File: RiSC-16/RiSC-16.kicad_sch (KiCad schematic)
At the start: 10 parts, among them U1 74LS283, U2 74LS00, U3 74LS175, U4 74LS257, U5 74LS175

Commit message: Added sheet for register file.
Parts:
- removed C1, C2, C3, C4, C5: 0.1 uF, symbol Device:C_Small_US
- removed U1: 74LS283, symbol 74xx:74LS283
- removed U2: 74LS00, symbol 74xx:74LS00
- removed U3, U5: 74LS175, symbol 74xx:74LS175
- removed U4: 74LS257, symbol 74xx:74LS257
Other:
- added sheet Register File (registers.kicad_sch)
- note removed: "ALU 4-bit slice Four required for ALU"

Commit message: Reworked ALU to use 74LS181 and control signals from Pro. Jacob's reference paper.
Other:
- added sheet Control Unit (control.kicad_sch)
- added sheet Sequencer (sequencer.kicad_sch)
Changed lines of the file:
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@@
+	)
+	(sheet
+		(at 3.81 688.34)
+		(size 290.83 205.74)
+		(exclude_from_sim no)
+		(in_bom yes)
+		(on_board yes)
+		(dnp no)
+		(fields_autoplaced yes)
+		(stroke
+			(width 0.1524)
+			(type solid)
+		)
+		(fill
+			(color 0 0 0 0.0000)
+		)
+		(property "Sheetname" "Sequencer"
+			(at 3.81 687.6284 0)
+			(effects
+				(font
+					(size 1.27 1.27)
+				)
+				(justify left bottom)
+			)
+		)
+		(property "Sheetfile" "sequencer.kicad_sch"
+			(at 3.81 894.6646 0)
+			(effects
+				(font
+					(size 1.27 1.27)
+				)
+				(justify left top)
+			)
+		)
+		(instances
+			(project "RiSC-16"
+				(path "/09ce4153-429f-4803-b069-3af485a81dd6"
+					(page "4")
+				)
+			)
+		)
+	)
+	(sheet
+		(at 5.08 918.21)
+		(size 295.91 195.58)
+		(exclude_from_sim no)
+		(in_bom yes)
+		(on_board yes)
+		(dnp no)
+		(fields_autoplaced yes)
+		(stroke
+			(width 0.1524)
+			(type solid)
+		)
+		(fill
+			(color 0 0 0 0.0000)
+		)
+		(property "Sheetname" "Control Unit"
+			(at 5.08 917.4984 0)
+			(effects
+				(font
+					(size 1.27 1.27)
+				)
+				(justify left bottom)
+			)
+		)
+		(property "Sheetfile" "control.kicad_sch"
+			(at 5.08 1114.3746 0)
+			(effects
+				(font
+					(size 1.27 1.27)
+				)
+				(justify left top)
+			)
+		)
+		(instances
+			(project "RiSC-16"
+				(path "/09ce4153-429f-4803-b069-3af485a81dd6"
+					(page "5")
+				)
+			)
+		)
 	)
 	(sheet

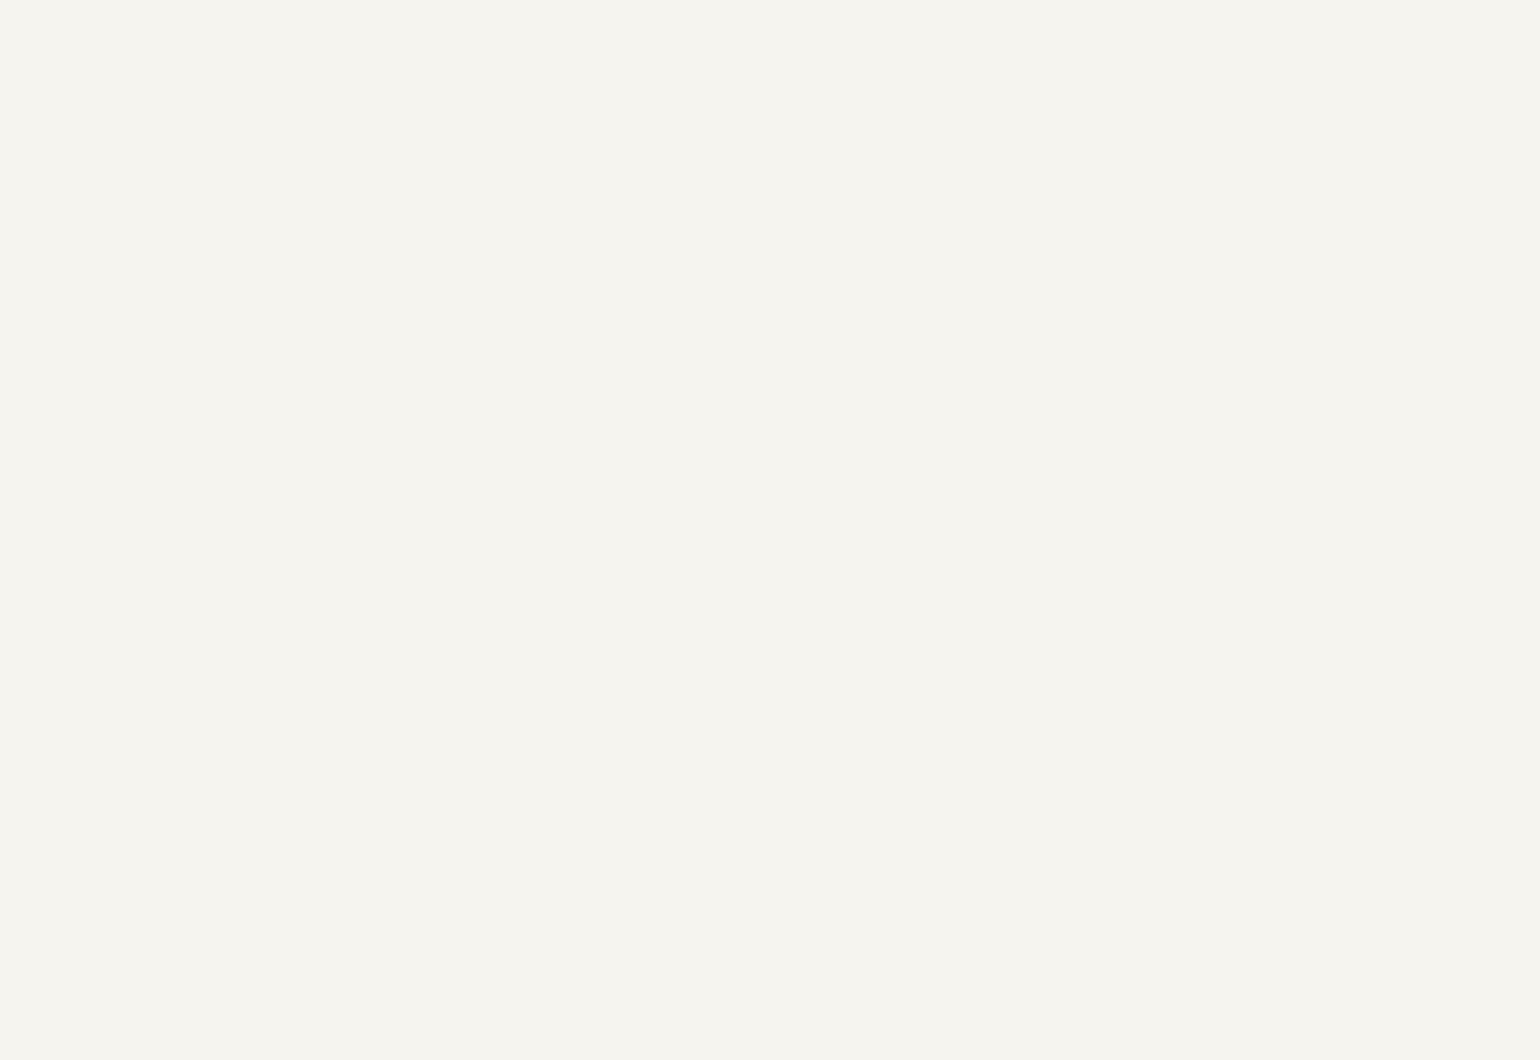
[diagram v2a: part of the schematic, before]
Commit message: Move program ccounter to its own page
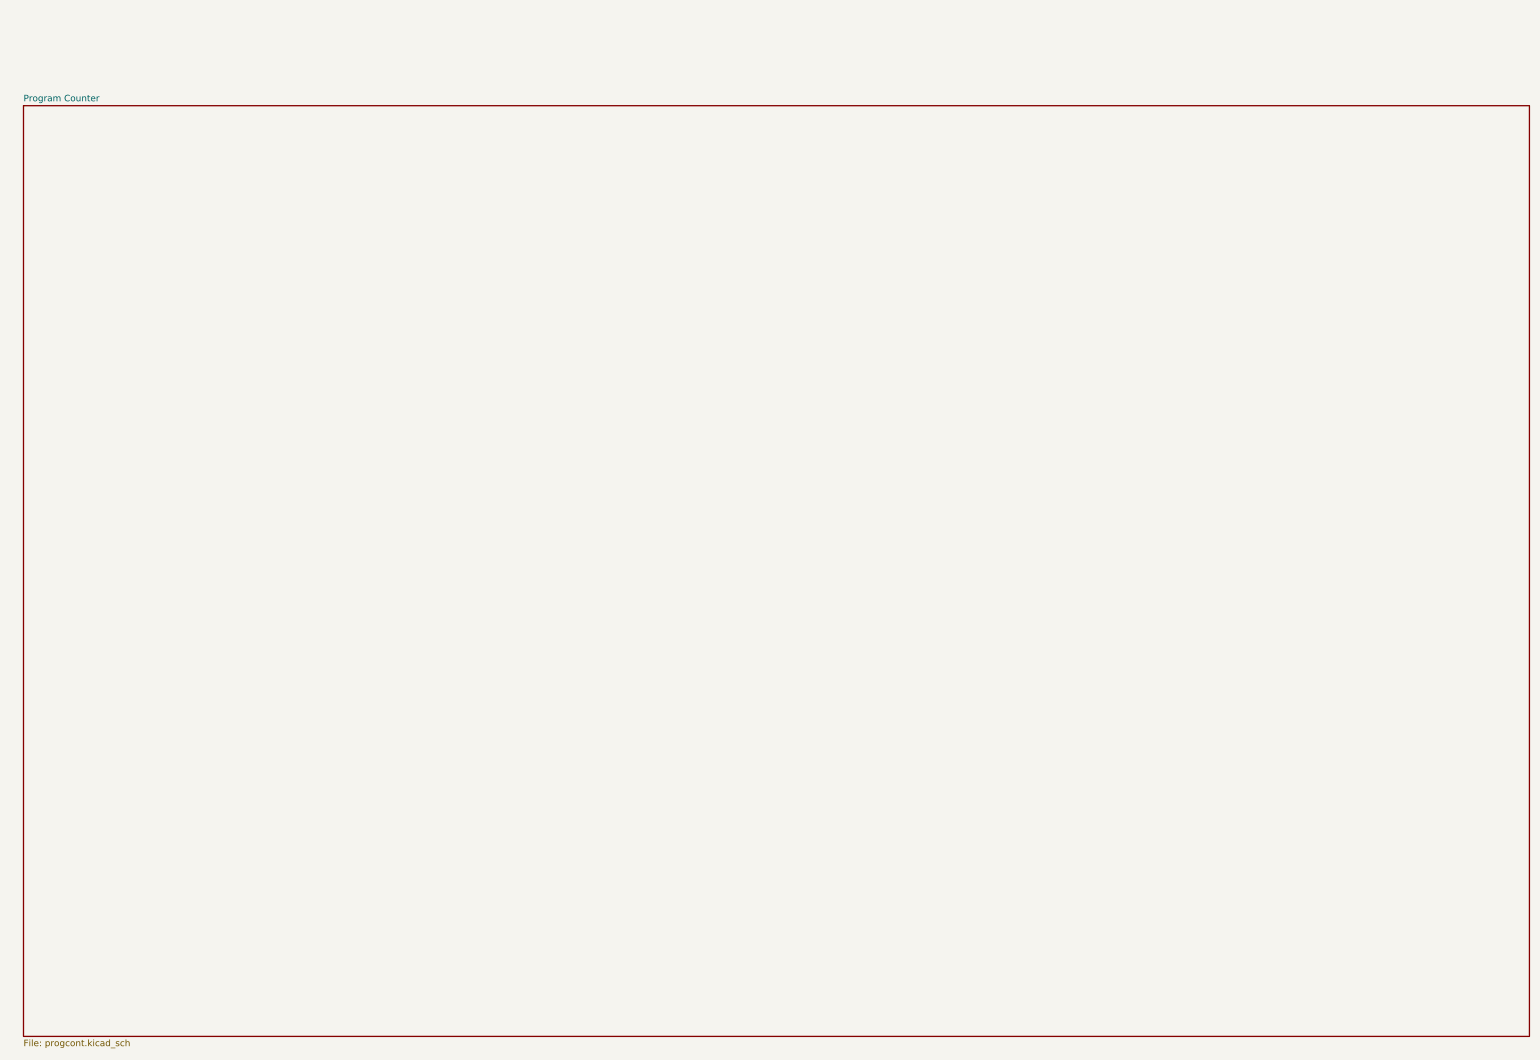
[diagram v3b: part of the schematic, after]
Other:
- added sheet Program Counter (progcont.kicad_sch)
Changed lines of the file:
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@@
 			(project "RiSC-16"
 				(path "/09ce4153-429f-4803-b069-3af485a81dd6"
-					(page "4")
+					(page "7")
 				)
 			)
@@
 				)
 			)
+		)
+	)
+	(sheet
+		(at 6.35 1140.46)
+		(size 295.91 182.88)
+		(exclude_from_sim no)
+		(in_bom yes)
+		(on_board yes)
+		(dnp no)
+		(fields_autoplaced yes)
+		(stroke
+			(width 0.1524)
+			(type solid)
+		)
+		(fill
+			(color 0 0 0 0.0000)
+		)
+		(property "Sheetname" "Program Counter"
+			(at 6.35 1139.7484 0)
+			(effects
+				(font
+					(size 1.27 1.27)
+				)
+				(justify left bottom)
+			)
+		)
+		(property "Sheetfile" "progcont.kicad_sch"
+			(at 6.35 1323.9246 0)
+			(effects
+				(font
+					(size 1.27 1.27)
+				)
+				(justify left top)
+			)
+		)
+		(instances
+			(project "RiSC-16"
+				(path "/09ce4153-429f-4803-b069-3af485a81dd6"
+					(page "4")
+				)
+			)

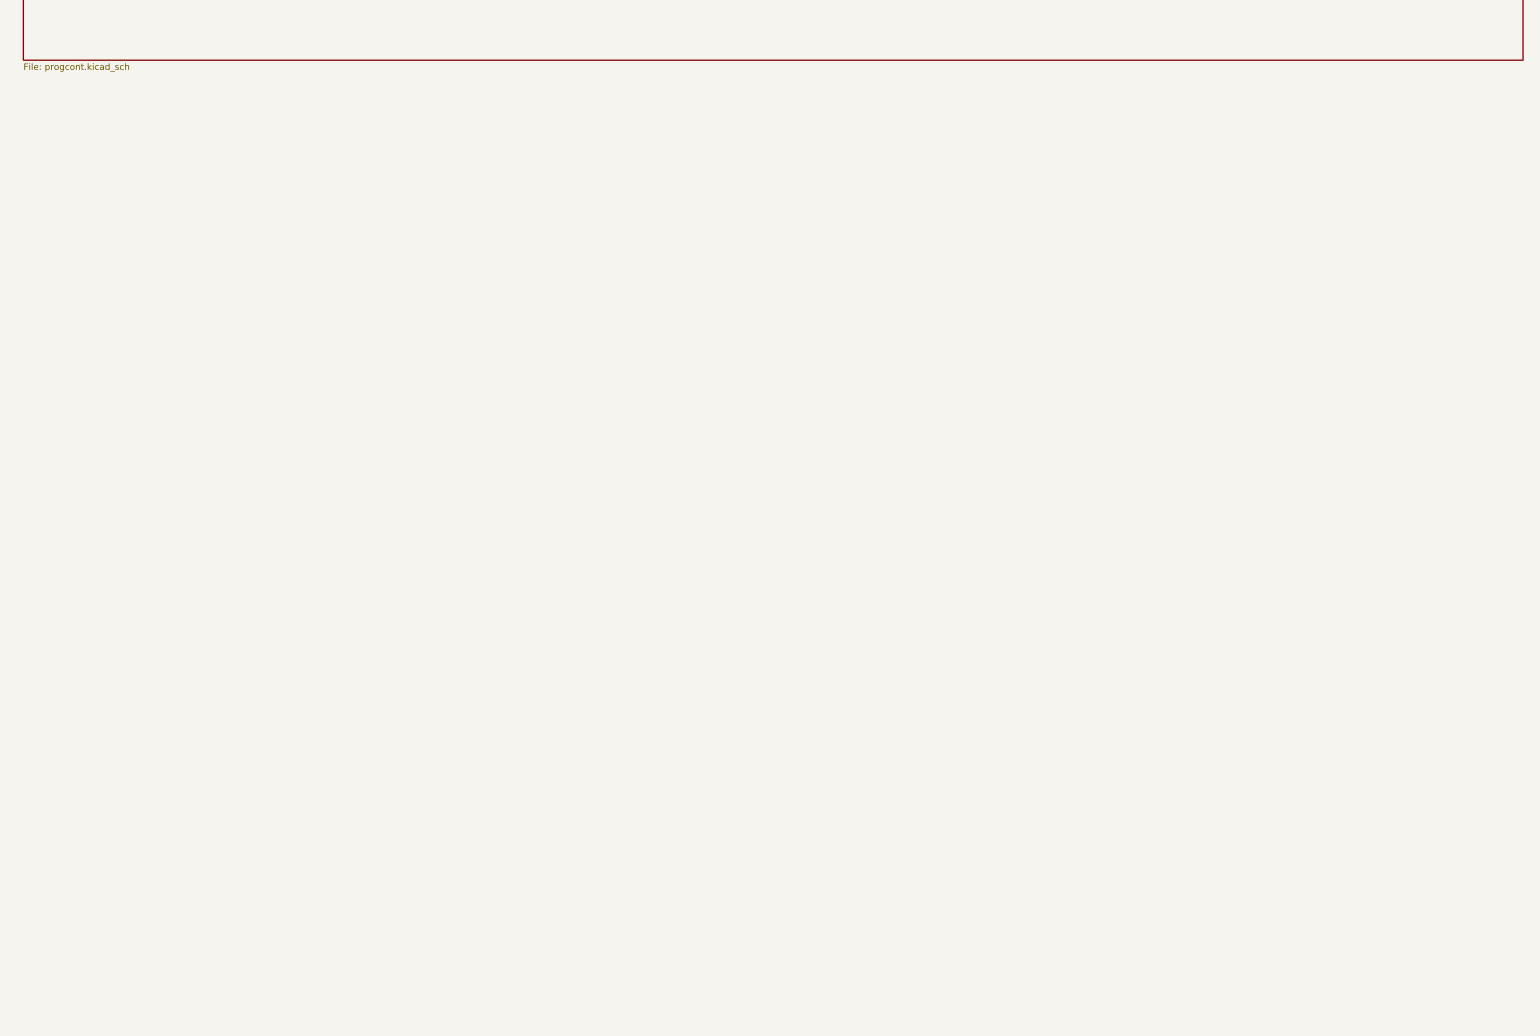
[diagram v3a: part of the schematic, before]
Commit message: Added a custom symbol for the AM29705. Reworked to use it in two different approaches.
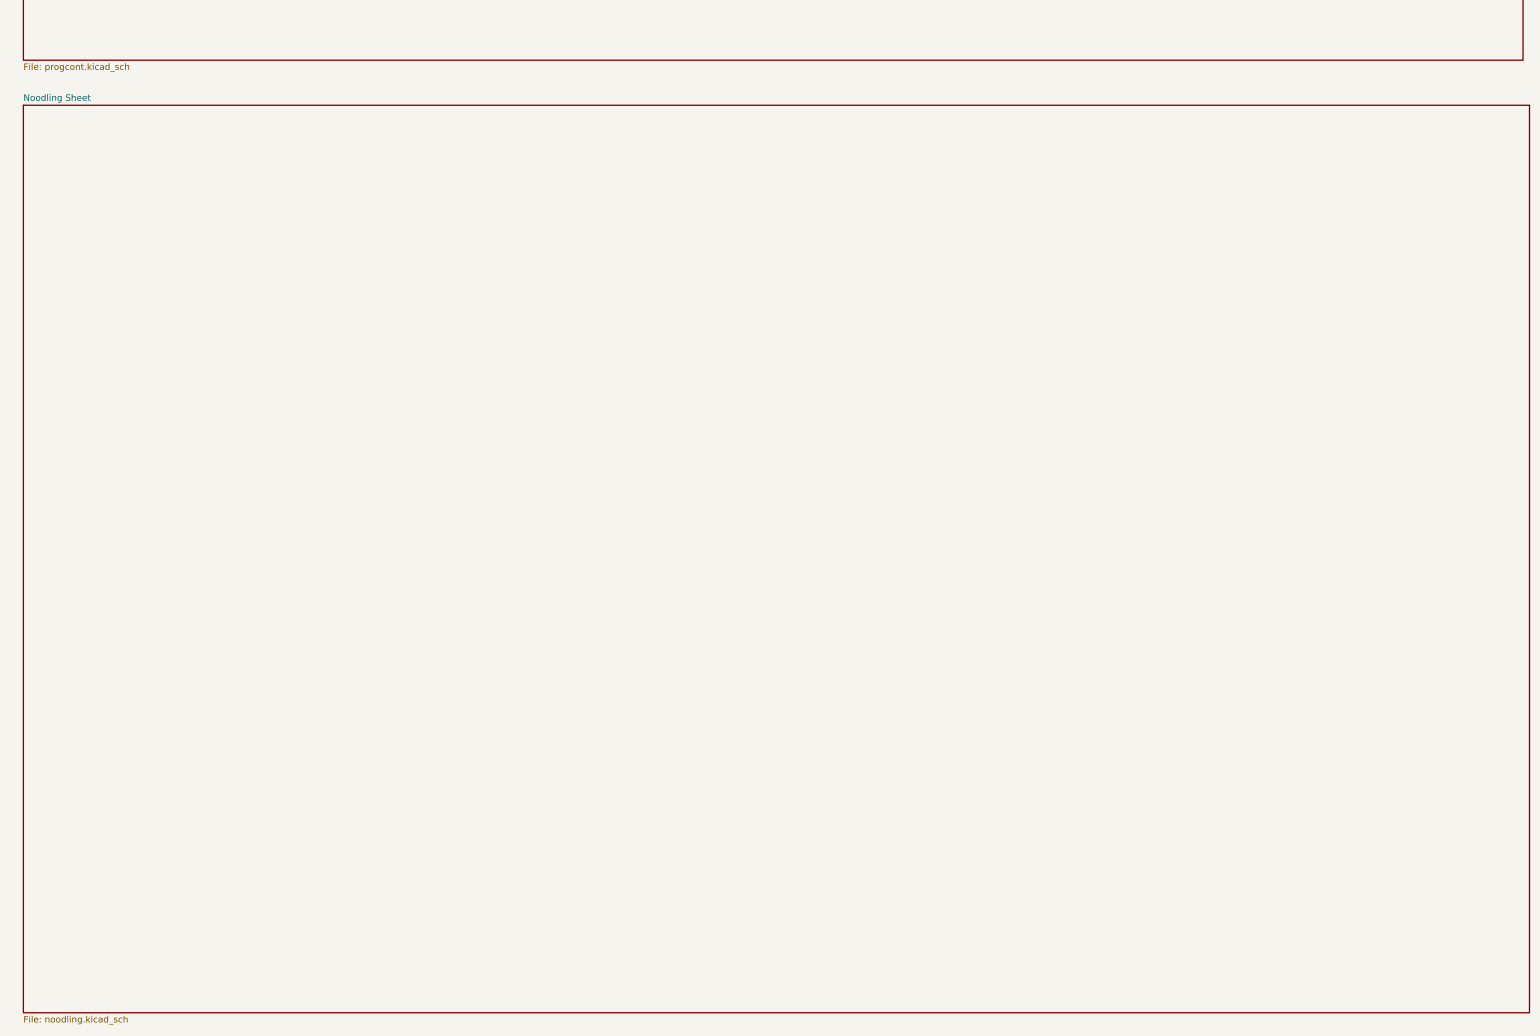
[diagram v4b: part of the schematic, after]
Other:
- added sheet Noodling Sheet (noodling.kicad_sch)
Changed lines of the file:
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@@
+	)
+	(sheet
+		(at 6.35 1332.23)
+		(size 297.18 179.07)
+		(exclude_from_sim no)
+		(in_bom yes)
+		(on_board yes)
+		(dnp no)
+		(fields_autoplaced yes)
+		(stroke
+			(width 0.1524)
+			(type solid)
+		)
+		(fill
+			(color 0 0 0 0.0000)
+		)
+		(property "Sheetname" "Noodling Sheet"
+			(at 6.35 1331.5184 0)
+			(effects
+				(font
+					(size 1.27 1.27)
+				)
+				(justify left bottom)
+			)
+		)
+		(property "Sheetfile" "noodling.kicad_sch"
+			(at 6.35 1511.8846 0)
+			(effects
+				(font
+					(size 1.27 1.27)
+				)
+				(justify left top)
+			)
+		)
+		(instances
+			(project "RiSC-16"
+				(path "/09ce4153-429f-4803-b069-3af485a81dd6"
+					(page "7")
+				)
+			)
+		)
 	)
 	(sheet
@@
 			(project "RiSC-16"
 				(path "/09ce4153-429f-4803-b069-3af485a81dd6"
-					(page "7")
+					(page "6")
 				)
 			)

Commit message: Moved and renamed pages.
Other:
- sheet ALU Slice renamed Register File and ALU
- sheet Program Counter renamed Instruction Register
- sheet Register File renamed EPROM and RAM
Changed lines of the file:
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@@
 			(color 0 0 0 0.0000)
 		)
-		(property "Sheetname" "ALU Slice"
+		(property "Sheetname" "Register File and ALU"
 			(at 5.08 226.6184 0)
 			(effects
@@
 			(color 0 0 0 0.0000)
 		)
-		(property "Sheetname" "Register File"
+		(property "Sheetname" "EPROM and RAM"
 			(at 5.08 459.0284 0)
 			(effects
@@
 			(color 0 0 0 0.0000)
 		)
-		(property "Sheetname" "Program Counter"
+		(property "Sheetname" "Instruction Register"
 			(at 6.35 1139.7484 0)
 			(effects
